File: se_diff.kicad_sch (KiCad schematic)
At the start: 12 parts

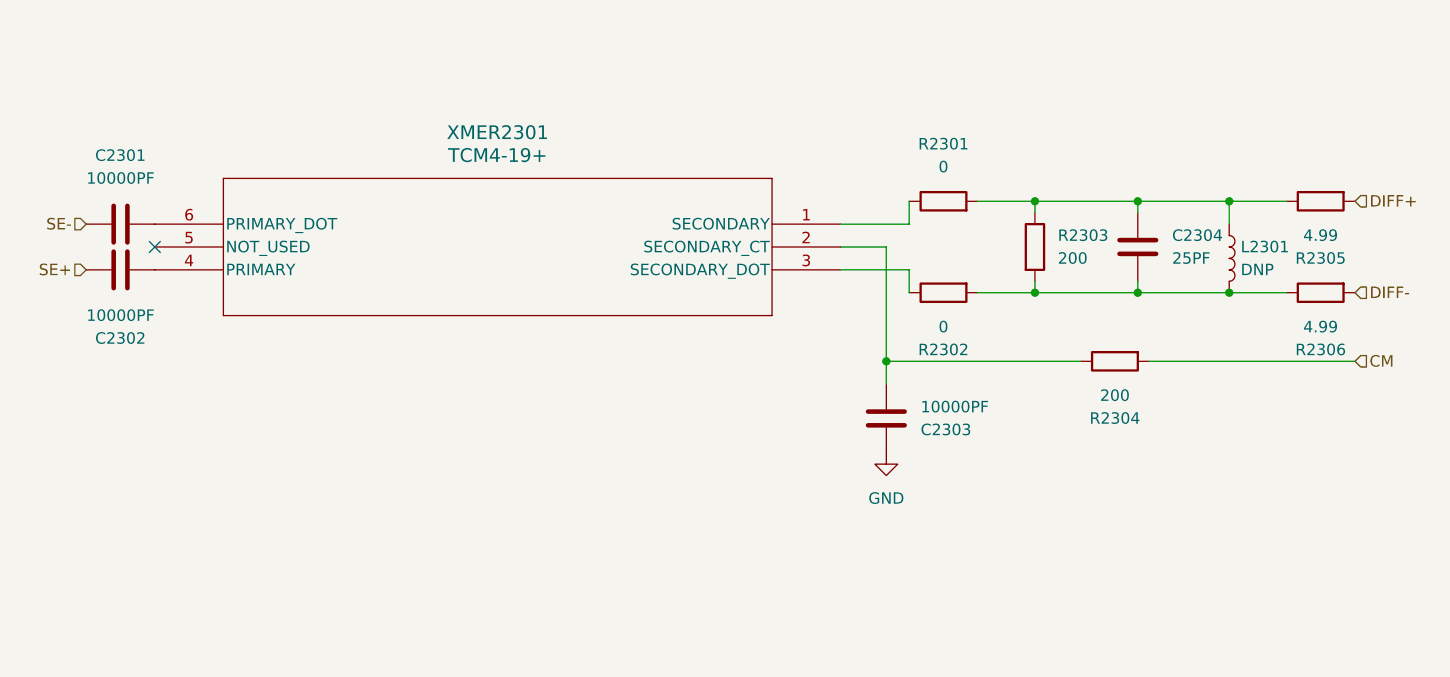
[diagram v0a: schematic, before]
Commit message: Changed RF filters for MPEX application
-Changed ADC filter from TCM4-19+ to TC1-1+
-Changed DAC filter from TCM4-19+ to TC4-6T+
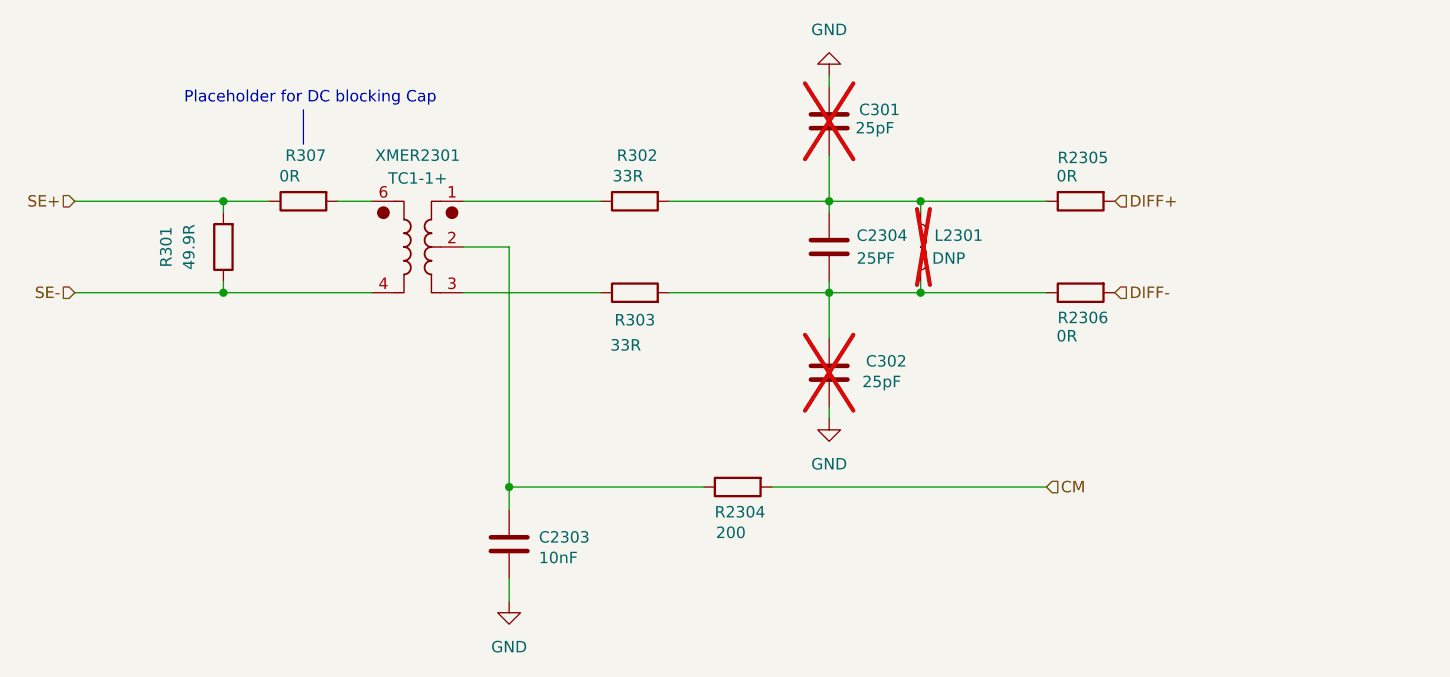
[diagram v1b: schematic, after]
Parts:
- removed C2301, C2302: 10000PF, Capacitor_SMD:C_0603_1608Metric, symbol Device:C
- removed R2301, R2302: 0, Resistor_SMD:R_0603_1608Metric, symbol Device:R
- removed R2303: 200, Resistor_SMD:R_0603_1608Metric, symbol Device:R
- removed XMER2301: TCM4-19+, 001_download:DB714_MNC, symbol 001_symbol:TCM4-19+
- added C301, C302: 25pF, Capacitor_SMD:C_0603_1608Metric, symbol Device:C
- added R301: 49.9R, Resistor_SMD:R_0603_1608Metric, symbol Device:R
- added R302, R303: 33R, Resistor_SMD:R_0603_1608Metric, symbol Device:R
- added R307: 0R, Resistor_SMD:R_0603_1608Metric, symbol Device:R
- added XMER2301: TC1-1+, Transformer_SMD:Transformer_MiniCircuits_AT224-1A, symbol Zest_Symbols:TC1-1+
- C2303: value 10000PF -> 10nF
- L2301: now not fitted
- R2305, R2306: value 4.99 -> 0R
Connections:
- net GND: now also C301.2, C302.1
- net SE+: now also R301.2, R307.1
- net SE-: now also R301.1, XMER2301.4
- net at C2304.2, L2301.2, R2306.1: now also C302.2, R303.2
- net at C2304.1, L2301.1, R2305.1: now also C301.1, R302.2
- net at C2303.2, R2304.1: now also XMER2301.2
- new net: R302.1, XMER2301.1
- new net: R303.1, XMER2301.3
- new net: R307.2, XMER2301.6
- no-connect marks 1 -> 0
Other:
- note added: "Placeholder for DC blocking Cap"
- moved on the sheet: C2303, C2304, R2304, R2305, R2306
